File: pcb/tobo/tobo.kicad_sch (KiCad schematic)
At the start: 95 parts, among them J1 54548-2272, J2 Conn_01x02_Pin, J4 54548-2472, J5 Conn_01x09_Pin, J6 Conn_01x09_Pin, J7 Conn_01x09_Pin, J8 Hroparts Elec TYPE-C-31-M-12, U1 TS5A23167DCUR, U10 5015, U11 5015, U12 5015, U13 5015, U14 CH340E, U15 5015, U16 5015, U17 TLV61220ADBVR, U2 ATmega328P-AN, U3 TS5A23167DCUR, U4 TS5A23167DCUR, U5 TS5A23167DCUR, U6 5015, U7 5015, U8 5015, U9 5015, X1 TestPoint, X2 TestPoint, X7 TestPoint, Y4 TestPoint

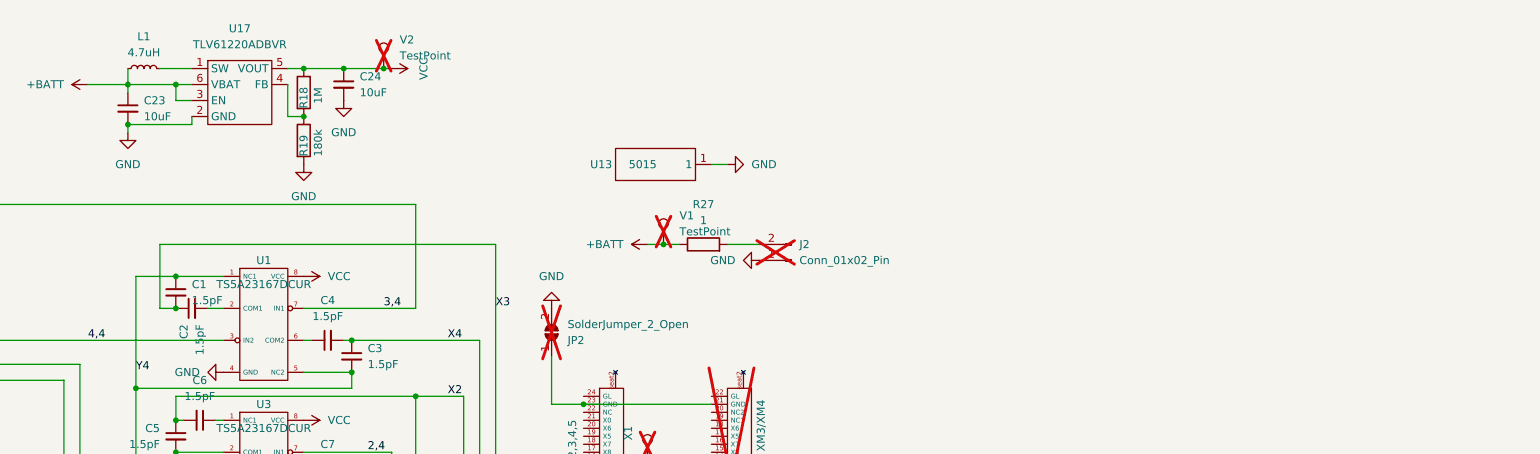
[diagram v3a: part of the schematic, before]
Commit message: Half-way to a better transformer
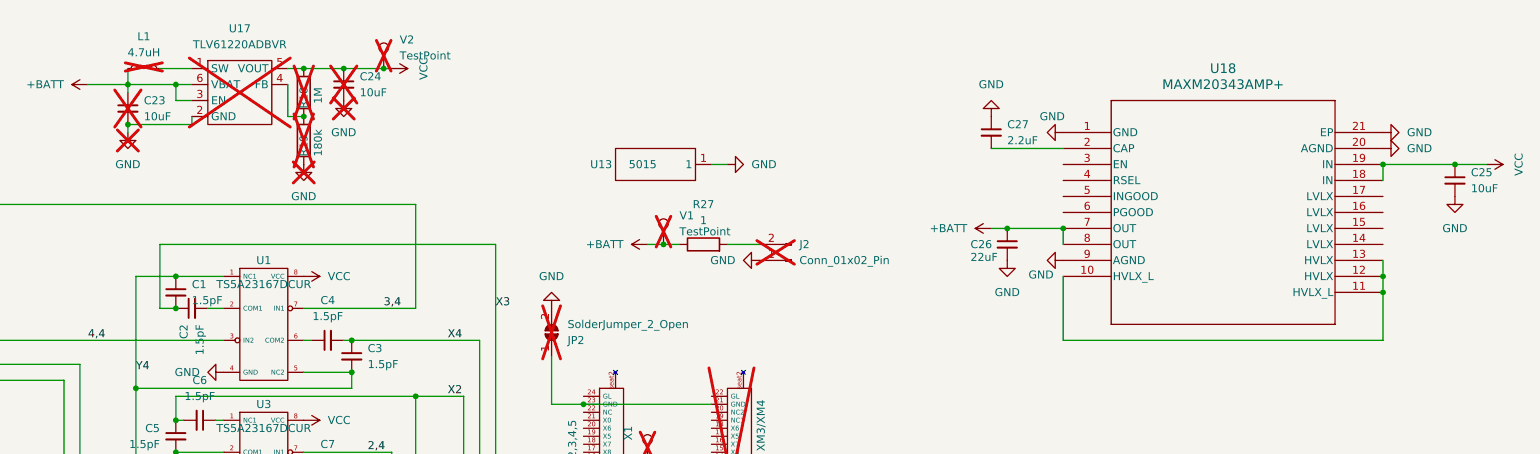
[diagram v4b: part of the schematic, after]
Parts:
- added C25: 10uF, Capacitor_SMD:C_0402_1005Metric, symbol Device:C_Small
- added C26: 22uF, Capacitor_SMD:C_0402_1005Metric, symbol Device:C_Small
- added C27: 2.2uF, Capacitor_SMD:C_0402_1005Metric, symbol Device:C_Small
- added U18: MAXM20343AMP+, tobo-footprints:21-100447_ADI, symbol tobo-components:MAXM20343AMP+
- C23, C24, L1, R18, R19, U17: now not fitted
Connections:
- net +BATT: now also C26.1, U18.7 (OUT), U18.8 (OUT)
- net GND: now also C25.2, C26.2, C27.1, U18.1 (GND), U18.20 (AGND), U18.21 (EP), U18.9 (AGND)
- net VCC: now also C25.1, U18.18 (IN), U18.19 (IN)
- new net: U18.10 (HVLX_L), U18.11 (HVLX_L), U18.12 (HVLX), U18.13 (HVLX)
- new net: C27.2, U18.2 (CAP)

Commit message: A mostly one-chip up- and down- converter.
This should work down to 0.5V, which is just a little bit over the low
battery warning of the headset.
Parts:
- C26: LCSC Part Number (none) -> C105226; Manufacturer_Part_Number (none) -> CL05A226MQ5QUNC
- C27: LCSC Part Number (none) -> C170151; Manufacturer_Part_Number (none) -> CL05A225KO5NQNC
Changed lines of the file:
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@@
 			)
 		)
-		(property "Manufacturer_Part_Number" ""
+		(property "Manufacturer_Part_Number" "CL05A225KO5NQNC"
 			(at 318.77 35.56 0)
 			(effects
@@
 			)
 		)
-		(property "LCSC Part Number" ""
+		(property "LCSC Part Number" "C170151"
 			(at 318.77 35.56 0)
 			(effects
@@
 			)
 		)
-		(property "Manufacturer_Part_Number" ""
+		(property "Manufacturer_Part_Number" "CL05A226MQ5QUNC"
 			(at 321.31 53.34 0)
 			(effects
@@
 			)
 		)
-		(property "LCSC Part Number" ""
+		(property "LCSC Part Number" "C105226"
 			(at 321.31 53.34 0)
 			(effects

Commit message: Minor versioning shenanigans
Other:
- moved on the sheet: C23, C24, L1, R18, R19, U17, V2

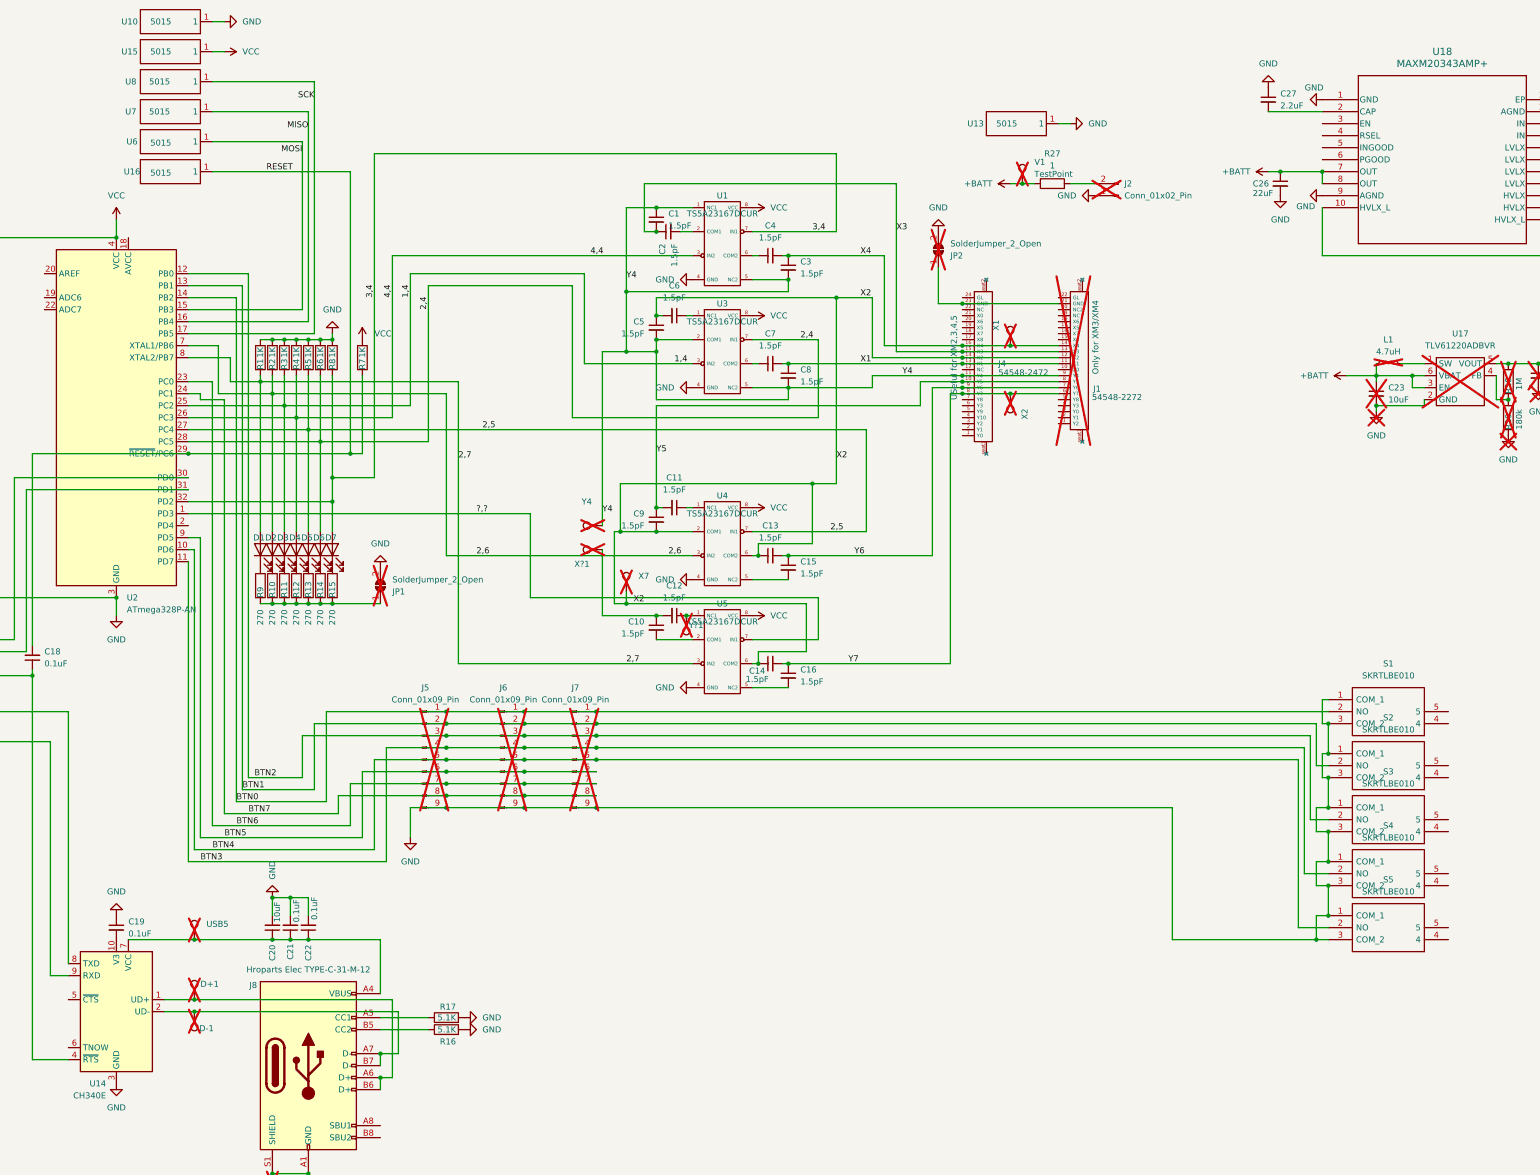
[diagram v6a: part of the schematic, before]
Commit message: Reworked PCB to use TC7MBL3125CFK bus switches
The old design didn't work, and I suspect it's due to the excessive
capacitance of the analog mux. This chip (~roughly) has been tested
against XM4s on the bench and works great with 1.5pF capacitors.
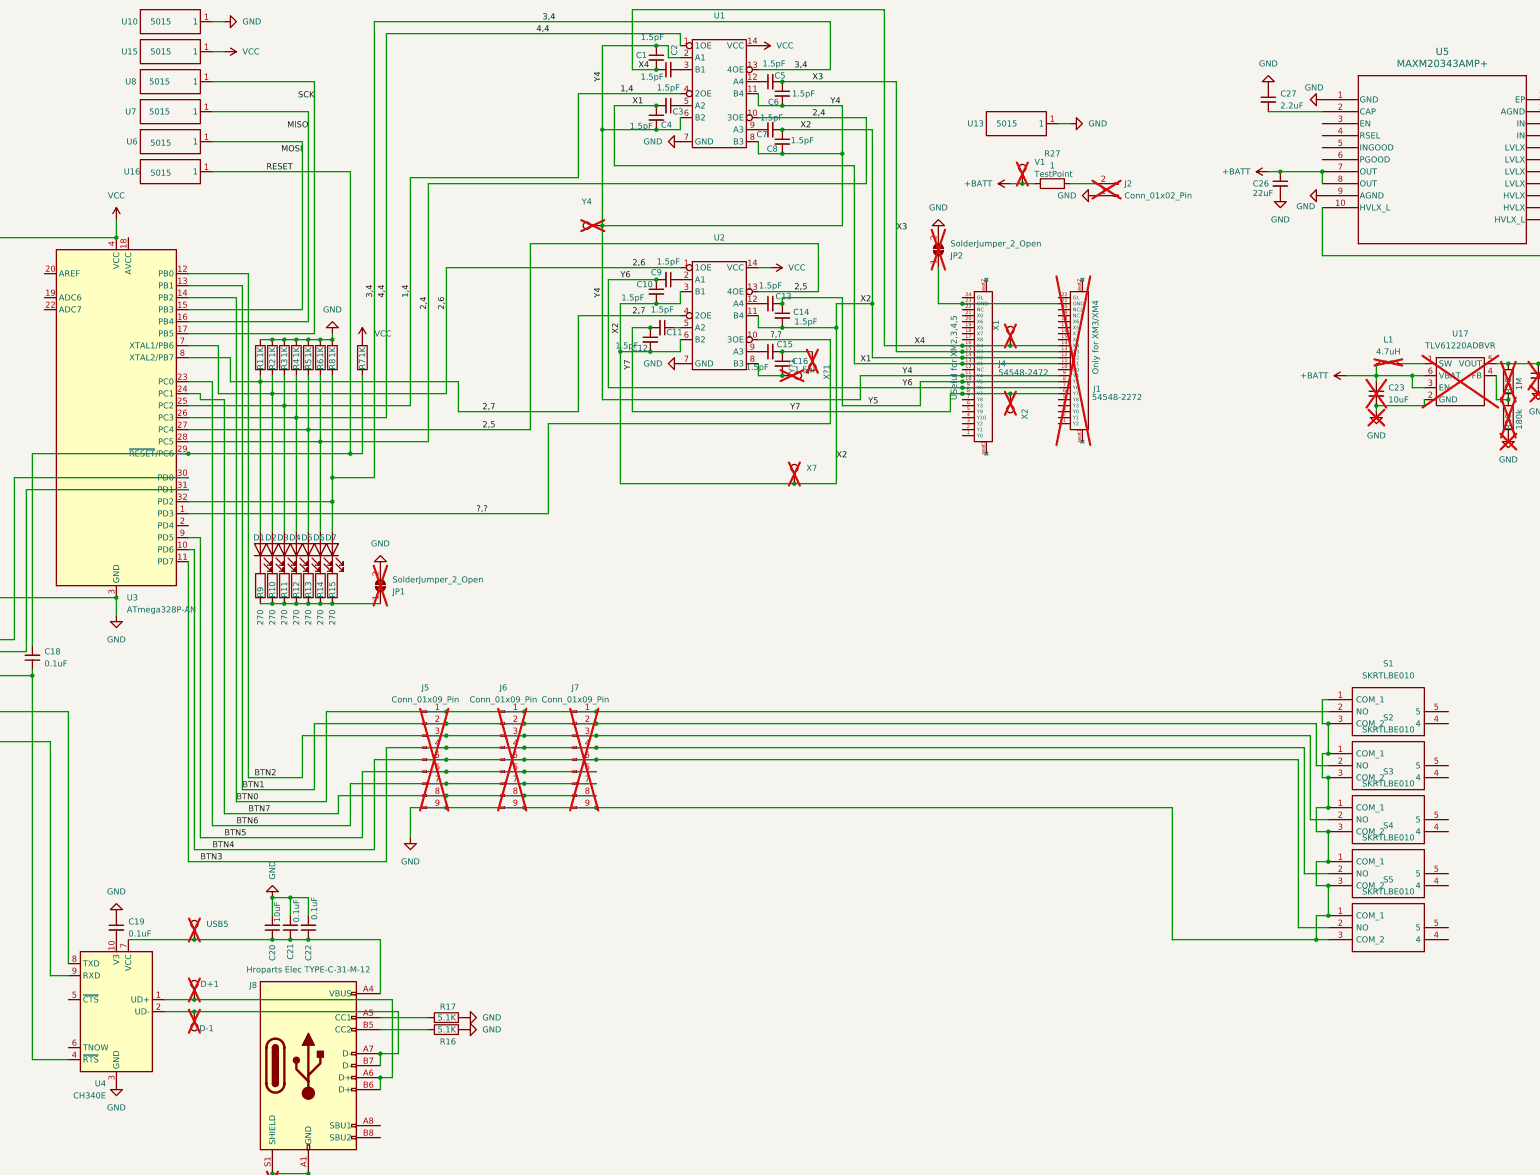
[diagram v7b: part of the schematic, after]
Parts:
- removed U1, U3, U4, U5: TS5A23167DCUR, tobo-footprints:VSSOP-8_2.3x2mm_P0.5mm_narrowpads, symbol tobo-components:tssa23167
- added U1, U2: ~, tobo-footprints:VSSOP50P400X100-14N, symbol tobo-components:TC7MBL3125CFK
- renumbered C9 to C10, C12 to C11, C10 to C12, C15 to C14, C14 to C15, C6 to C3, C5 to C4, C4 to C5, C3 to C6, C11 to C9, U2 to U3, U14 to U4, U18 to U5
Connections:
- net 1,4: now also U1.4 (2OE)
- net 2,4: now also U1.10 (3OE)
- net 2,5: now also U2.13 (4OE)
- net 2,6: now also U2.1 (1OE)
- net 2,7: now also U2.4 (2OE)
- net 3,4: now also U1.13 (4OE)
- net 4,4: now also U1.1 (1OE)
- net ?,?: now also U2.10 (3OE)
- net GND: now also U1.7 (GND), U2.7 (GND)
- net VCC: now also U1.14 (VCC), U2.14 (VCC)
- net X1: now also C3.2, C4.1; no longer C7.2, C8.1
- net X2: now also C12.2, C14.2, C7.2, C8.1, U2.11 (B4), U2.3 (B1), U2.6 (B2); no longer C13.1, C15.1, C3.2, C4.1
- net X3: now also C5.2, C6.1; no longer C1.2, C2.1
- net X4: now also C1.2, C2.1; no longer C5.2, C6.1
- net Y4: now also U1.11 (B4), U1.2 (A1), U1.6 (B2), U1.8 (B3)
- net Y5: now also C13.2, C14.1; no longer C10.1, C9.2
- net Y6: now also C10.1, C9.2; no longer C13.2, C14.1
- net Y7: now also C11.2, C12.1; no longer C15.2, C16.1
- net at Y?1.1: now also C16.2, U2.8 (B3); no longer C11.1
- net at C3.1: now also U1.5 (A2)
- net at C7.1: now also U1.9 (A3)
- net at C9.1: now also U2.2 (A1)
- net at C5.1: now also U1.12 (A4)
- net at C2.2: now also U1.3 (B1)
- new net: C15.2, C16.1, X?1.1
- new net: C11.1, U2.5 (A2)
- new net: C15.1, U2.9 (A3)
- new net: C13.1, U2.12 (A4)
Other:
- moved on the sheet: C1, C10, C11, C12, C13, C14, C15, C16, C2, C3, C4, C5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

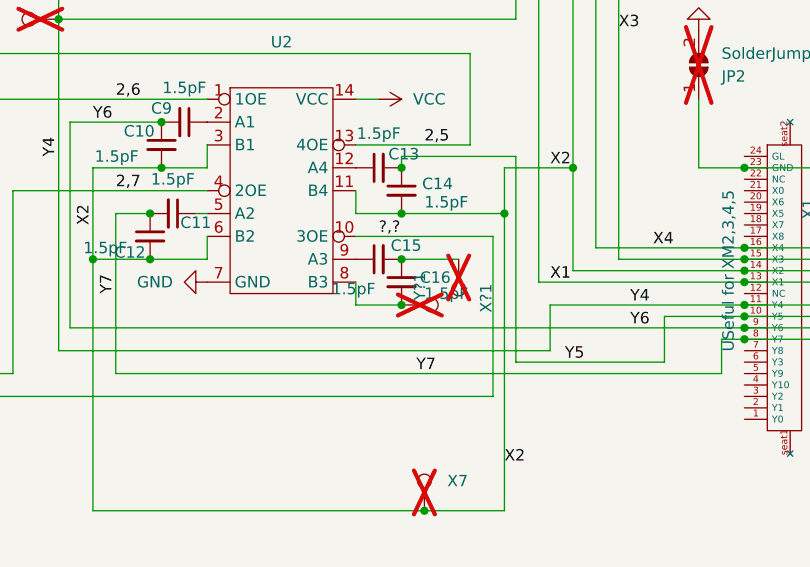
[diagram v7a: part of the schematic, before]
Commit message: Unused controller now has through-hole caps for experimentation
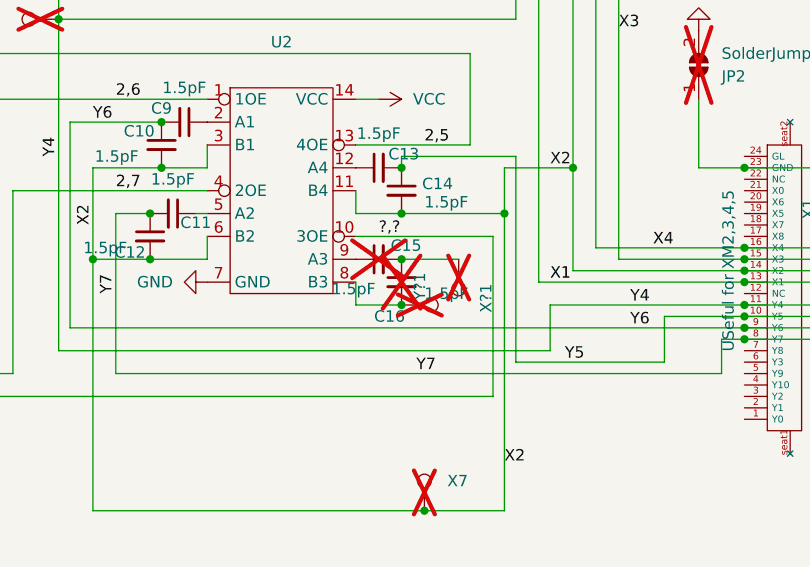
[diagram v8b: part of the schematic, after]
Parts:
- C15, C16: footprint Capacitor_SMD:C_0402_1005Metric -> Capacitor_THT:C_Disc_D5.0mm_W2.5mm_P2.50mm; now not fitted; now left out of the parts list
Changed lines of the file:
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@@
 		(unit 1)
 		(exclude_from_sim no)
-		(in_bom yes)
-		(on_board yes)
-		(dnp no)
+		(in_bom no)
+		(on_board yes)
+		(dnp yes)
 		(property "Reference" "C15"
 			(at 216.408 87.376 90)
@@
 			)
 		)
-		(property "Footprint" "Capacitor_SMD:C_0402_1005Metric"
+		(property "Footprint" "Capacitor_THT:C_Disc_D5.0mm_W2.5mm_P2.50mm"
 			(at 213.36 88.9 0)
 			(effects
@@
 		(unit 1)
 		(exclude_from_sim no)
-		(in_bom yes)
-		(on_board yes)
-		(dnp no)
+		(in_bom no)
+		(on_board yes)
+		(dnp yes)
 		(property "Reference" "C16"
-			(at 217.932 90.932 0)
+			(at 212.852 95.25 0)
 			(effects
 				(font
@@
 			)
 		)
-		(property "Footprint" "Capacitor_SMD:C_0402_1005Metric"
+		(property "Footprint" "Capacitor_THT:C_Disc_D5.0mm_W2.5mm_P2.50mm"
 			(at 215.9 91.44 0)
 			(effects
